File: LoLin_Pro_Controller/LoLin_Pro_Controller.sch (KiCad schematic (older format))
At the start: 25 parts, among them J1 Conn_01x03, J10 Volt_Sel, J2 Conn_01x03, J3 Conn_01x03, J4 Conn_01x03, J5 Conn_01x03, J6 Conn_01x03, M1 LolinD32, U2 LM7805_TO220, U3 SN74HCT245N

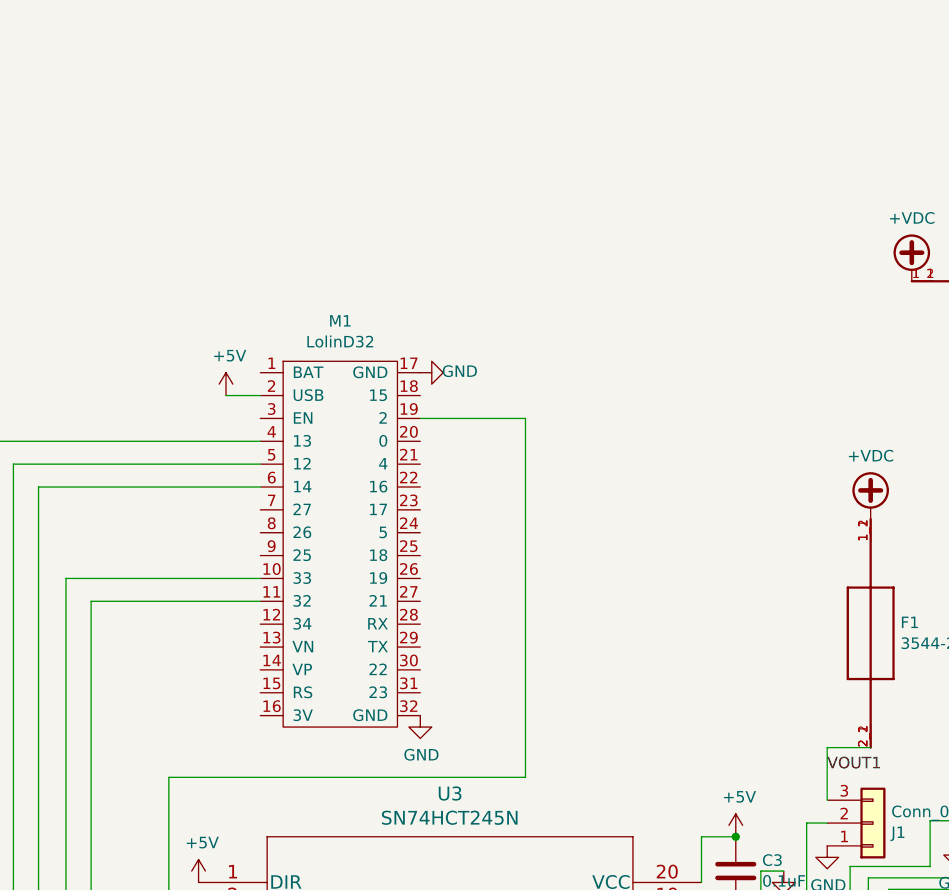
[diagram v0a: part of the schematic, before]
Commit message: added OLED
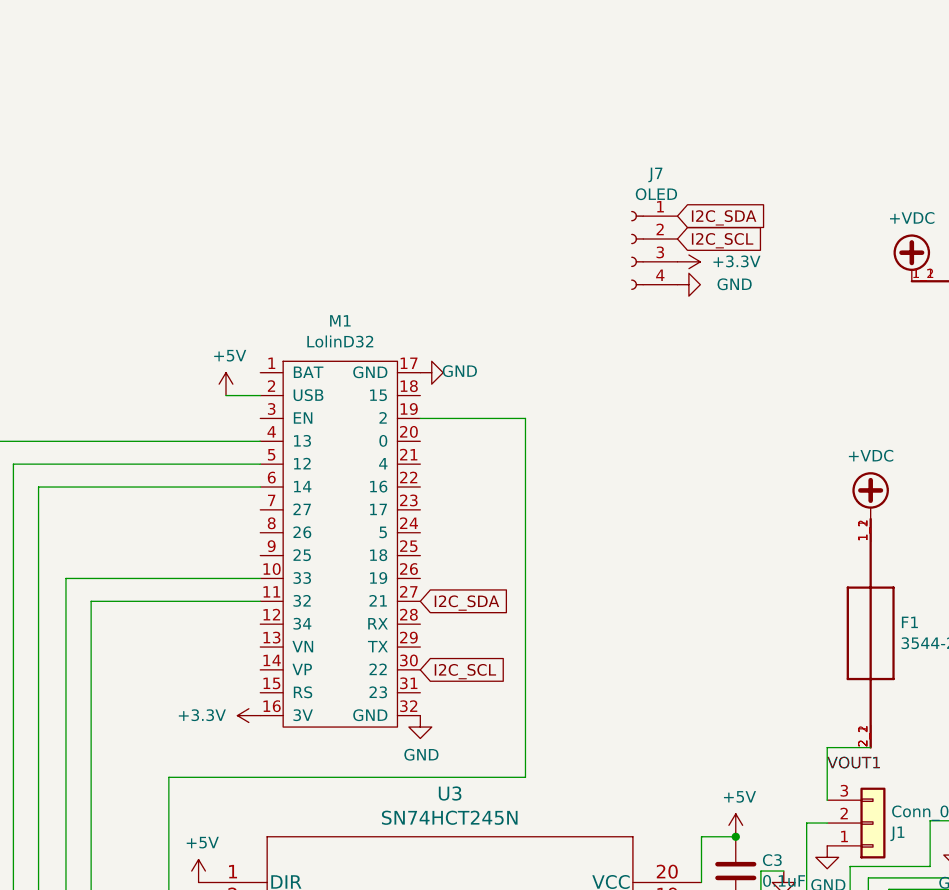
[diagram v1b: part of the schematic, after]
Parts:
- added J7: OLED, OLED-SSD1306-128X64-I2C:OLED-SSD1306-128X64-I2C-THT, symbol Connector:Conn_01x04_Female
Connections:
- net GND: now also J7.4 (Pin_4)
- net +3V3: now reaches M1.16 (3V)
- net +3V3: now also J7.3 (Pin_3)
- net I2C_SDA: now reaches M1.27 (21)
- net I2C_SDA: now also J7.1 (Pin_1)
- net I2C_SCL: now reaches M1.30 (22)
- net I2C_SCL: now also J7.2 (Pin_2)
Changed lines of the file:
@@
 Sheet 1 1
 Title "Lolin Pro Controller"
-Date "2021-09-07"
-Rev "v1"
+Date "2021-09-23"
+Rev "v2"
 Comp ""
 Comment1 ""
@@
 Wire Wire Line
 	2780 4870 3360 4870
+$Comp
+L Connector:Conn_01x04_Female J7
+U 1 1 614DFC49
+P 5255 1755
+F 0 "J7" H 5147 2040 50  0000 C CNN
+F 1 "OLED" H 5147 1949 50  0000 C CNN
+F 2 "OLED-SSD1306-128X64-I2C:OLED-SSD1306-128X64-I2C-THT" H 5255 1755 50  0001 C CNN
+F 3 "~" H 5255 1755 50  0001 C CNN
+	1    5255 1755
+	-1   0    0    -1
+$EndComp
+Text GLabel 5455 1655 2    50   Input ~ 0
+I2C_SDA
+Text GLabel 5455 1755 2    50   Input ~ 0
+I2C_SCL
+$Comp
+L power:GND #PWR08
+U 1 1 614E8F64
+P 5455 1955
+F 0 "#PWR08" H 5455 1705 50  0001 C CNN
+F 1 "GND" V 5455 1705 50  0000 C CNN
+F 2 "" H 5455 1955 50  0001 C CNN
+F 3 "" H 5455 1955 50  0001 C CNN
+	1    5455 1955
+	0    -1   -1   0
+$EndComp
+$Comp
+L power:+3.3V #PWR07
+U 1 1 614ECE34
+P 5455 1855
+F 0 "#PWR07" H 5455 1705 50  0001 C CNN
+F 1 "+3.3V" V 5455 2005 50  0000 L CNN
+F 2 "" H 5455 1855 50  0001 C CNN
+F 3 "" H 5455 1855 50  0001 C CNN
+	1    5455 1855
+	0    1    1    0
+$EndComp
+$Comp
+L power:+3.3V #PWR09
+U 1 1 614F1EC8
+P 3630 3840
+F 0 "#PWR09" H 3630 3690 50  0001 C CNN
+F 1 "+3.3V" V 3630 3990 50  0000 L CNN
+F 2 "" H 3630 3840 50  0001 C CNN
+F 3 "" H 3630 3840 50  0001 C CNN
+	1    3630 3840
+	0    -1   -1   0
+$EndComp
+Text GLabel 4330 3340 2    50   Input ~ 0
+I2C_SDA
+Text GLabel 4330 3640 2    50   Input ~ 0
+I2C_SCL
 $EndSCHEMATC
